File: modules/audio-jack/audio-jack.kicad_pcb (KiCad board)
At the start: 2 copper layers, 1 part, among them J1 SJ-43514-SMT-TR

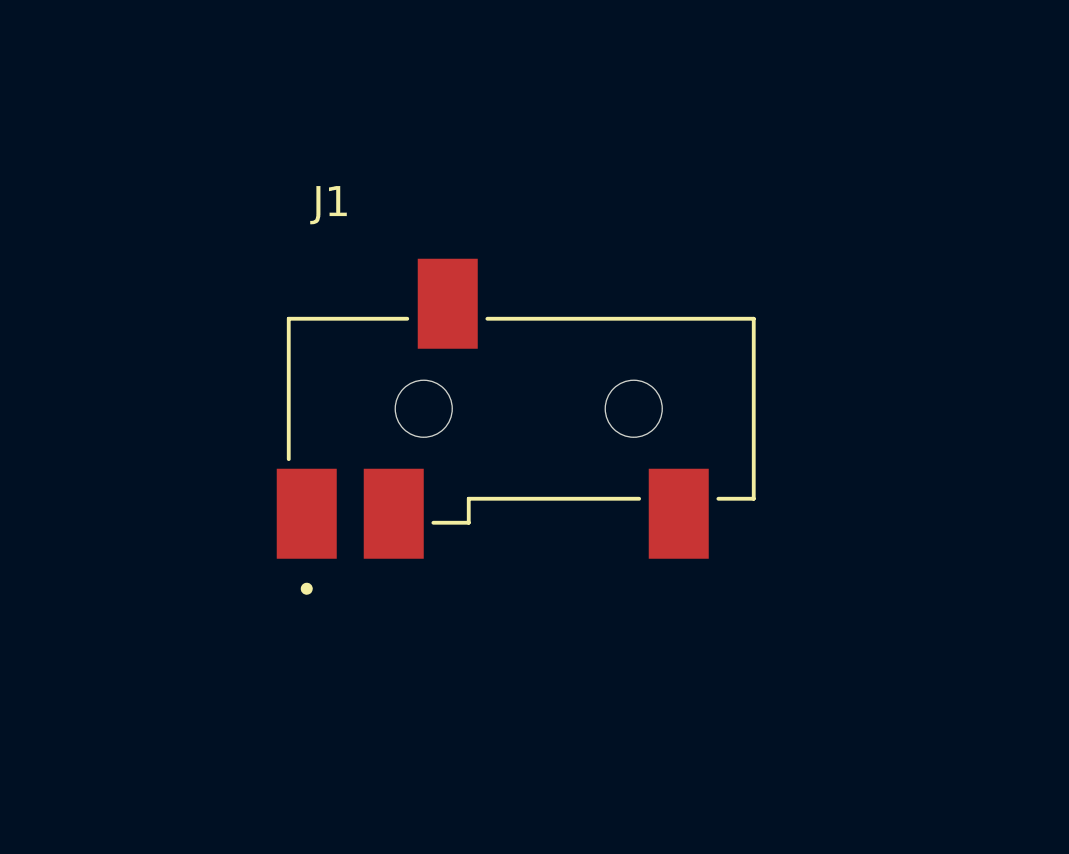
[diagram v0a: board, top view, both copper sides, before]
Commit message: finish audio jack module
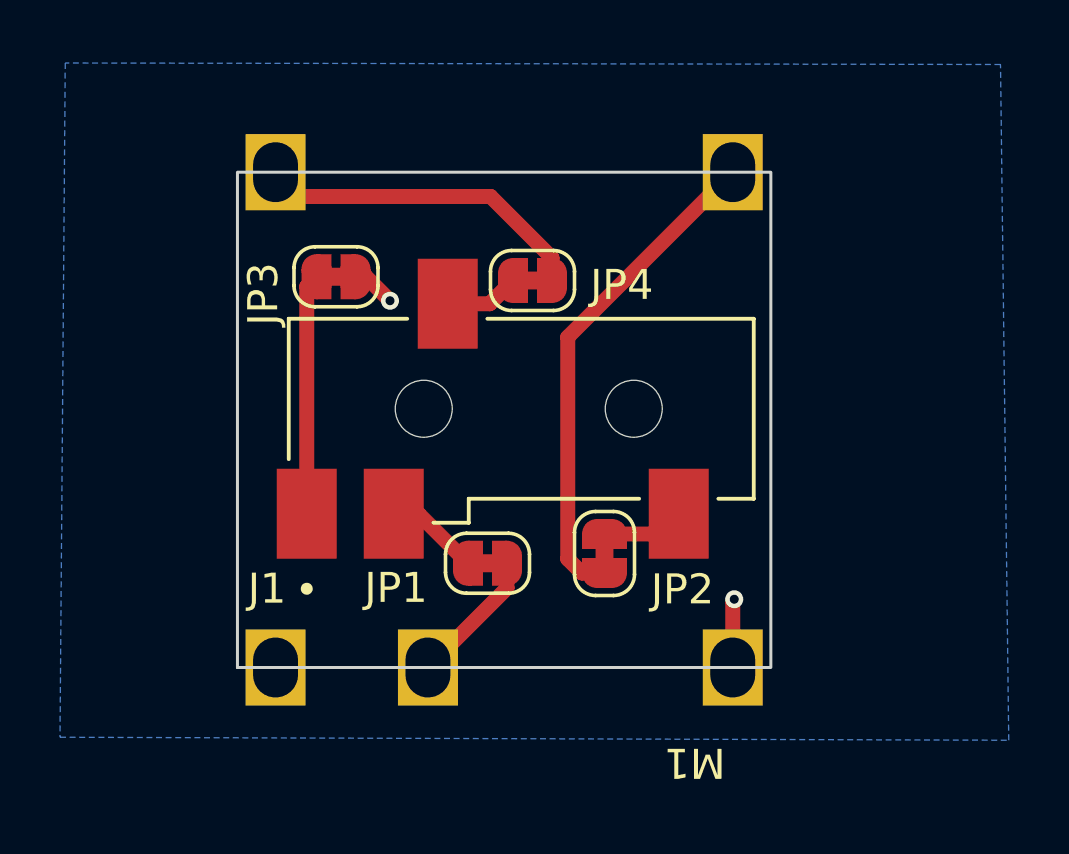
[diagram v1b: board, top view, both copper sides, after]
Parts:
- added JP1: Jumper_2_Bridged, Jumper:SolderJumper-2_P1.3mm_Bridged_RoundedPad1.0x1.5mm, F.Cu at (46.6, 41.6)
- added JP2: Jumper_2_Bridged, Jumper:SolderJumper-2_P1.3mm_Bridged_RoundedPad1.0x1.5mm, F.Cu at (50.5, 41.3)
- added JP3: Jumper_2_Bridged, Jumper:SolderJumper-2_P1.3mm_Bridged_RoundedPad1.0x1.5mm, F.Cu at (41.6, 32.1)
- added JP4: Jumper_2_Bridged, Jumper:SolderJumper-2_P1.3mm_Bridged_RoundedPad1.0x1.5mm, F.Cu at (48.1, 32.2)
- added M1: ~, MegaCastle:MegaCastle2x7-Module-I12.7x11.5-MA304, F.Cu at (51.0, 36.9)
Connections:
- J1 pad 1: unconnected-(J1-Pad1) -> Net-(JP3-A)
- J1 pad 2: unconnected-(J1-Pad2) -> Net-(JP2-B)
- J1 pad 3: unconnected-(J1-Pad3) -> Net-(JP4-B)
- J1 pad 4: unconnected-(J1-Pad4) -> Net-(JP1-A)
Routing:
- net RIGHT: track 0.00 -> 16.6 mm
- net LEFT: track 0.00 -> 11.2 mm
- net Net-(JP3-A): track 0.00 -> 8.03 mm
- net MIC: track 0.00 -> 5.20 mm
- net GND: track 0.00 -> 3.78 mm, vias 0 -> 2
- net Net-(JP1-A): track 0.00 -> 3.16 mm
- net Net-(JP2-B): track 0.00 -> 2.75 mm
- net Net-(JP4-B): track 0.00 -> 2.50 mm
- added copper zone on B.Cu, net GND
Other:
- board outline added: 17.8 x 16.5 mm
- board text added: "audio-jack r20250214 github.com/ gardners/ megaphone-r5 -modular"

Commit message: update audio-jack PCB to include panel
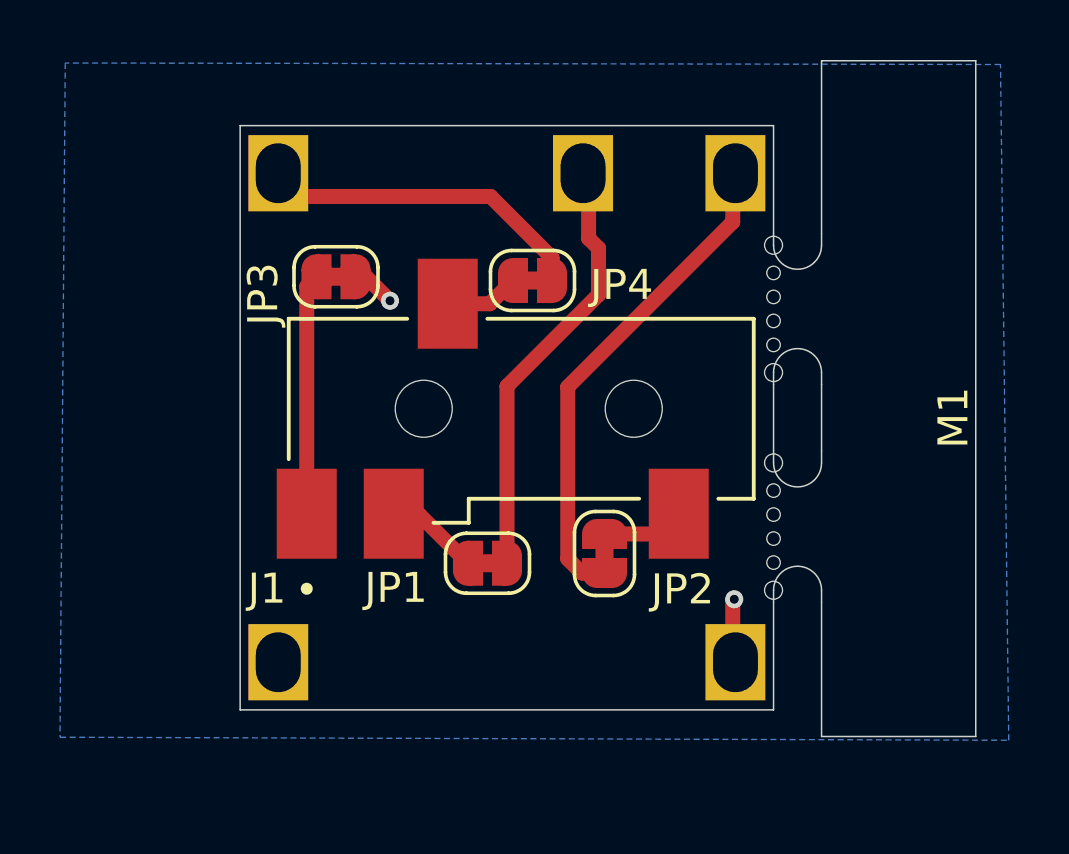
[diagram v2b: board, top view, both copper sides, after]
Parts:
- M1: footprint MegaCastle:MegaCastle2x7-Module-I12.7x11.5-MA304 -> MegaCastle:MegaCastle2x7-Module-I12.7x13.0-M8314-PANEL-NIBBLE
- moved M1 3.72 mm to (47.3, 36.8)
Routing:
- net MIC: track 5.20 -> 14.4 mm
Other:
- board size 17.8 x 16.5 mm -> 19.4 x 19.5 mm
- board text added: "audio-jack r20250219 github.com/ gardners/ megaphone-r5 -modular"
- board text removed: "audio-jack r20250214 github.com/ gardners/ megaphone-r5 -modular"
